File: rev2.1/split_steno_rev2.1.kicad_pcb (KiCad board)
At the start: 2 copper layers, 99.7 x 74.8 mm, 76 parts, among them J1 USB_OTG, J1 USB_mini_micro_B, J2 Audio-Jack-4, J3 Conn_01x03, P1 TC2030-IDC, SW1 SW_Push, SW10 SW_Push, SW11 SW_Push, SW12 SW_Push, SW13 SW_Push, SW14 SW_Push, SW15 SW_Push, SW16 SW_Push, SW17 SW_Push, SW18 SW_Push, SW19 SW_Push, SW2 SW_Push, SW20 SW_Push, SW21 SW_Push, SW22 Switch-6P-2S2T, SW3 SW_Push, SW4 SW_Push, SW5 SW_Push, SW6 SW_Push, SW7 SW_Push, SW8 SW_Push, SW9 SW_Push, U1 74LVC1G34, U4 MCP1700, U5 ATXMEGA128A4U-AU, U6 nRF24L01_module

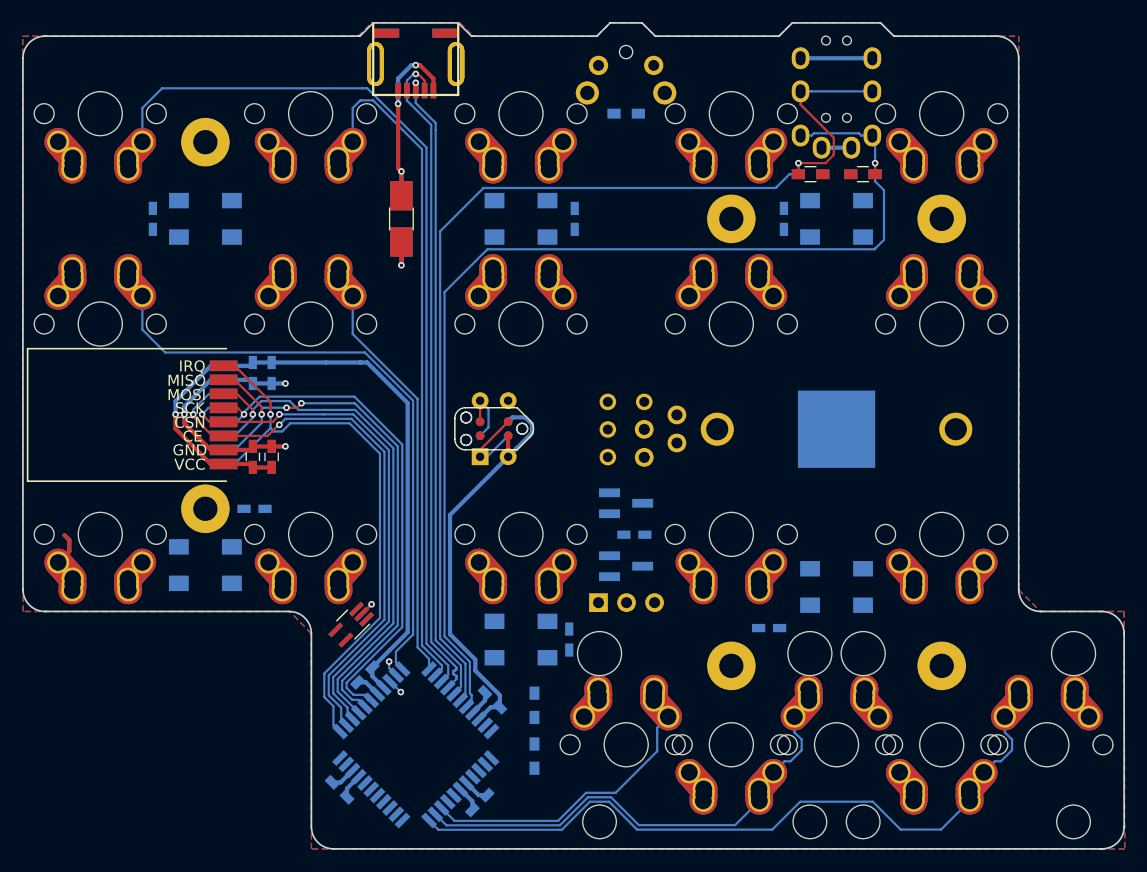
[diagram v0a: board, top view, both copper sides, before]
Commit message: filled in back gnd plane
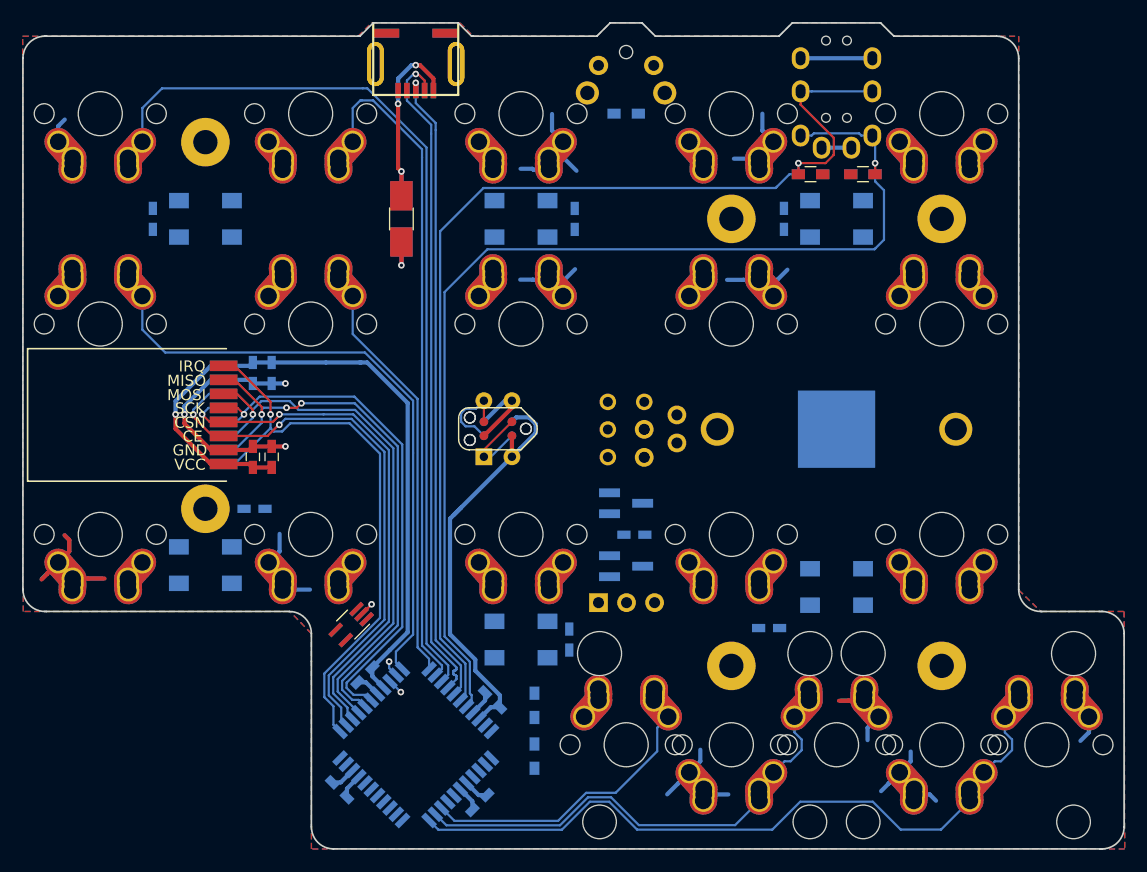
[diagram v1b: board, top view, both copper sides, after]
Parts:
- moved P1 0.34 mm to (76.5, 102.3)
- moved TC2030-NL 0.34 mm to (76.5, 102.4)
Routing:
- net GND: track 45.0 -> 120.0 mm
- net /RST: track 5.72 -> 7.80 mm
- net VCC: track 107.4 -> 108.4 mm

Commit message: added keepout under nrf module
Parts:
- added LED?: VAL**, WS2812B:WS2812B, F.Cu at (50.0, 114.7)
- added LED?: VAL**, WS2812B:WS2812B, F.Cu at (50.0, 83.3)
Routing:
- net GND: track 120.0 -> 52.1 mm
- net Net-(LED1-Pad2): track 0.00 -> 33.1 mm
